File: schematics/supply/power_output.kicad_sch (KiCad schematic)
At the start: 41 parts, among them Q10 IRLML0030, U2 EL817, U23 TL331, U24 INA169, U9 IRS2153S

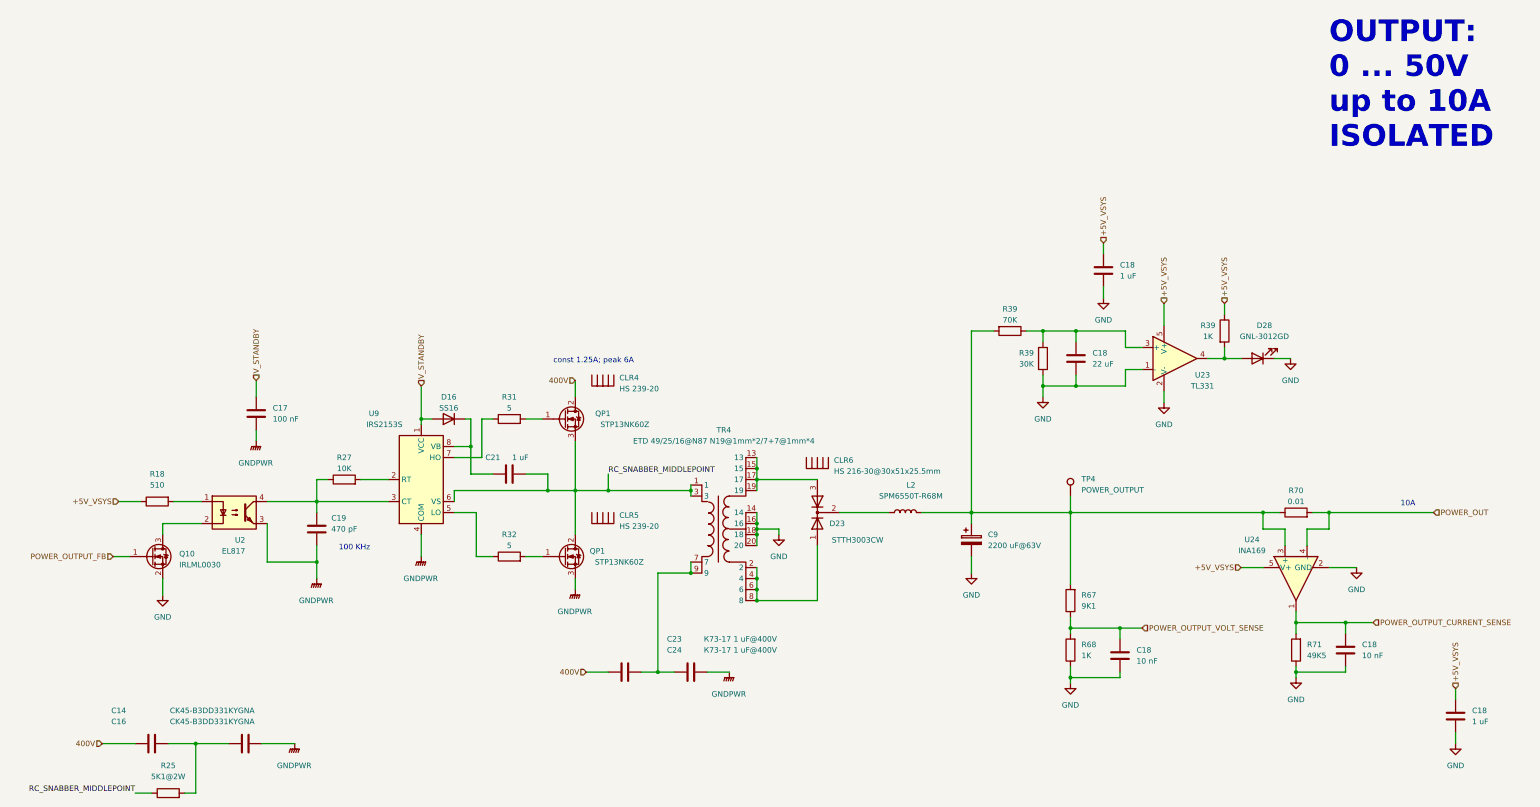
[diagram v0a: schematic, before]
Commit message: UV board size changed to 100x100 to reduce production price
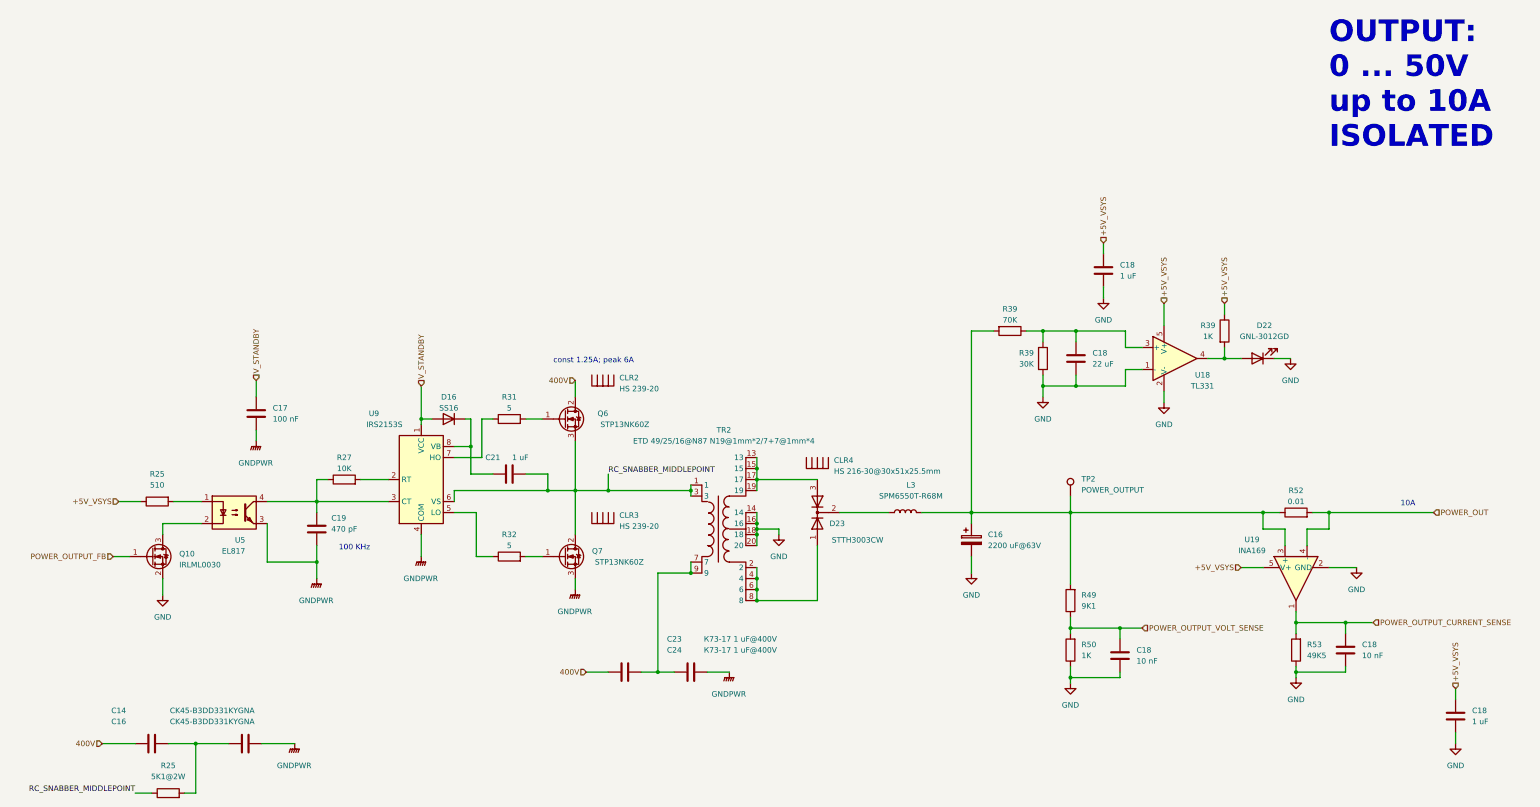
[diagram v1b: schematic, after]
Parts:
- renumbered C9 to C16, CLR4 to CLR2, CLR5 to CLR3, CLR6 to CLR4, D28 to D22, L2 to L3, QP1 to Q6, QP1 to Q7, R18 to R25, R67 to R49, R68 to R50, R70 to R52, R71 to R53, TP4 to TP2, TR4 to TR2, U23 to U18, U24 to U19, U2 to U5
